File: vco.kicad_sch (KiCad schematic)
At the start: 84 parts, among them J2 Conn_01x18_Pin, Q5 PN2222A, Q6 BC309, Q7 BC309, Q8 BC239, SW2 SW_Rotary_1x3_MP, U10 4013, U14 74LS221, U16 LF353, U20 LF351N, U21 LM301, U22 LM301, U23 LM741

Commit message: Extract keyboard
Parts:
- removed C28: 22uF, symbol Device:C_Polarized
- removed C29: 0.1uF, symbol Device:C
- removed J2: Conn_01x18_Pin, symbol Connector:Conn_01x20_Pin
- removed R73: 33R, symbol Device:R
- removed R74: 100R, symbol Device:R
- removed R75: 3K3, symbol Device:R
- removed RV23: 22K, symbol Device:R_Potentiometer_Trim
- removed U17: ~, symbol Analog:SGS-M110
- RV22: value R_Potentiometer -> 100KA
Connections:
- net +12V: now also U21.7 (V+)
- net -12V: now also U21.4 (V-)
- net at U21.1 (BAL): now also C37.2
- net 2': now reaches U18.2
- net 4': now reaches U18.3
- net 8': now reaches U18.4
- net 16': now reaches U18.5
- net at R95.1: now also U18.9; no longer U18.8
- net at R94.1: now also U18.8; no longer U18.9
- net DC: now reaches Q6.1 (C), Q6.2 (B), Q7.2 (B)
- net at R92.1: now also U18.7; no longer U18.10
- no-connect marks 22 -> 16
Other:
- note added: "5% PWM"
- note added: "CLOCK"
- note added: "LINEARITY"
- note added: "WAVEFORM"
- note removed: "V.REG."
- moved on the sheet: C24, C25, C26, C27, C30, C31, C32, C33, C34, C35, C36, C37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

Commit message: Add missing values and connectors
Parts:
- removed U23: LM741, symbol Amplifier_Operational:LM741
- added J7: Conn_01x11_Pin, symbol Connector:Conn_01x11_Pin
- added U26: LM741, symbol PCM_Amplifier_Operational_AKL:OPAMP_8-pin_Generic
- C24, C25: value C -> 22pF
- R100, R102: value 100K -> 10K
- R70, R90: value 10R -> 10K
- R72: value 36K -> 5K6
- R84: value 47K -> 10K
- R85, R86: value 47K -> 100K
- RV30: value 100KA -> 10KA
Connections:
- net +12V: now also R85.1, J7.1 (Pin_1), U26.7 (V+); no longer R85.2
- net +5V: now also J7.2 (Pin_2)
- net -12V: now also J7.4 (Pin_4), U26.4 (V-)
- net 16': now also J7.11 (Pin_11)
- net 2': now also J7.8 (Pin_8)
- net 4': now also J7.9 (Pin_9)
- net 8': now also J7.10 (Pin_10)
- net CLOCK: now also J7.5 (Pin_5)
- net DC: now also J7.7 (Pin_7)
- net GLIDE: now also J7.6 (Pin_6)
- net GND: now also C31.2, R102.1, J7.3 (Pin_3); no longer C31.1, R102.2
- net at R100.2, R101.1: now also U26.6
- net at R84.2, R86.2, U20.3 (+): now also R85.2; no longer R85.1
- net at R101.2, R103.2, R104.2: now also U26.2 (-)
- net at R69.1, R70.2, U14.7 (RCext): now also C25.2; no longer C25.1
- net at U14.6 (Cext): now also C25.1; no longer C25.2
- net at R77.2, U10.2 (~{Q}): now also C35.1, R90.2
- net PWM renamed PULSE
- new net: C31.1, R77.1, U10.6 (S)
- new net: R102.2, U26.3 (+)
- no-connect marks 16 -> 14
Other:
- note added: "GLIDE"
- note added: "PULSE WIDTH"
- moved on the sheet: C24, C25, C26, C27, C30, C31, C32, C33, C34, C35, C36, D9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

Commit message: Assign footprints and start PCB
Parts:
- C24, C25, C26, C30, C31, C32, C33, C34, C35, C36, C37: footprint (none) -> Capacitor_THT:C_Disc_D5.0mm_W2.5mm_P5.00mm
- CP27: renamed from C27; footprint (none) -> Capacitor_THT:CP_Radial_D8.0mm_P3.80mm
- J7: footprint (none) -> Connector_PinHeader_2.54mm:PinHeader_1x11_P2.54mm_Vertical
- R100, R101, R102, R103, R104, R105, R65, R66, R67, R68, R69, R70, R71, R72, R76, R77, R78, R79, R80, R81, R82, R83, R84, R85, R86, R87, R88, R89, R90, R91, R92, R93, R94, R95, R96, R97, R98, R99: footprint (none) -> Resistor_THT:R_Axial_DIN0204_L3.6mm_D1.6mm_P7.62mm_Horizontal
- RT20: renamed from RV20; footprint (none) -> Potentiometer_THT:Potentiometer_Bourns_3339P_Vertical_HandSoldering
- RT21: renamed from RV21; footprint (none) -> Potentiometer_THT:Potentiometer_Bourns_3339P_Vertical_HandSoldering
- RT26: renamed from RV26; footprint (none) -> Potentiometer_THT:Potentiometer_Bourns_3339P_Vertical_HandSoldering
- RT27: renamed from RV27; footprint (none) -> Potentiometer_THT:Potentiometer_Bourns_3339P_Vertical_HandSoldering
- RT28: renamed from RV28; footprint (none) -> Potentiometer_THT:Potentiometer_Bourns_3339P_Vertical_HandSoldering
- RV19, RV22, RV24, RV25, RV29, RV30: footprint (none) -> Potentiometer_THT:Potentiometer_Omeg_PC16BU_Vertical
- SW2: footprint (none) -> Button_Switch_THT:SR2511F-0403-(L)K0A-C9-S-3_1
- SW40: renamed from U18; value ~ -> 2P4T; footprint (none) -> Button_Switch_THT:SR2511F-0204-(L)K0A-C9-S-3
- U10: footprint (none) -> Package_DIP:DIP-14_W7.62mm_LongPads
- U14: footprint (none) -> Package_DIP:DIP-16_W10.16mm_LongPads
- U16, U26: footprint (none) -> Package_DIP:DIP-8_W7.62mm_LongPads
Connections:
- net GLIDE: no longer J7.6 (Pin_6)
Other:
- note added: "LEVEL"

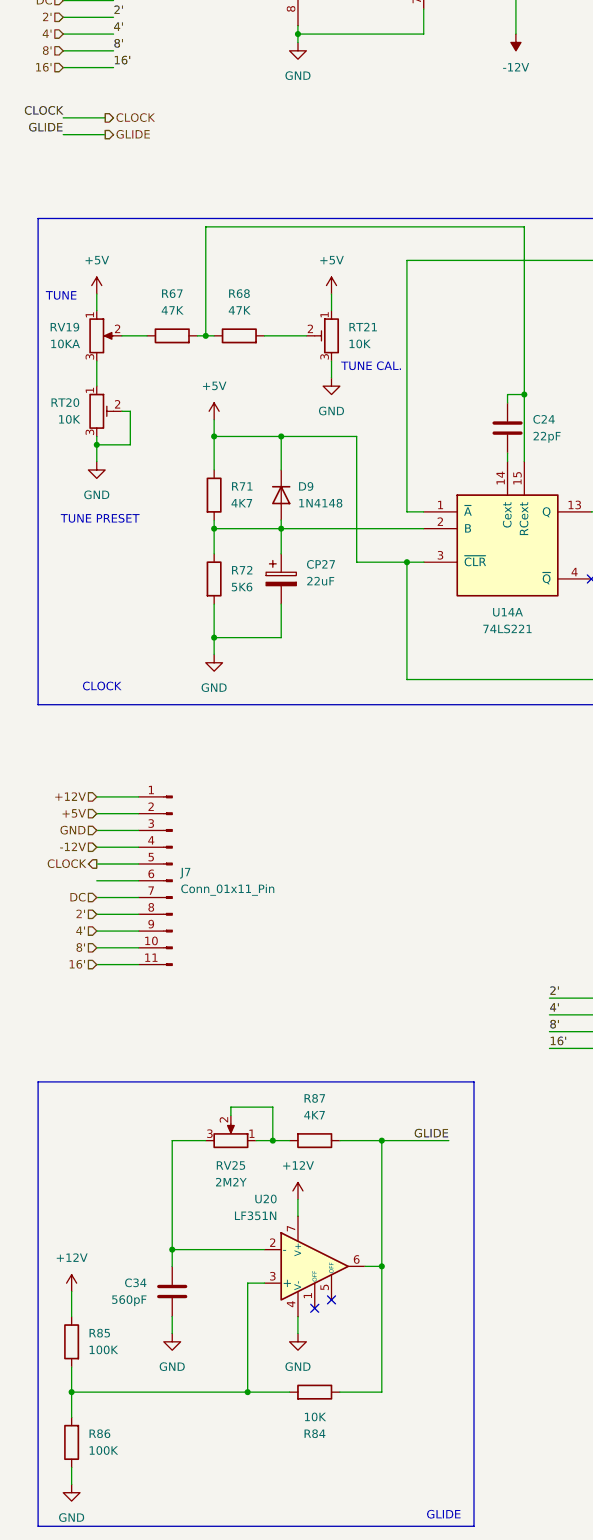
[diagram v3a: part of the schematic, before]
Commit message: Added layout photos, noise & ADSR components are in position
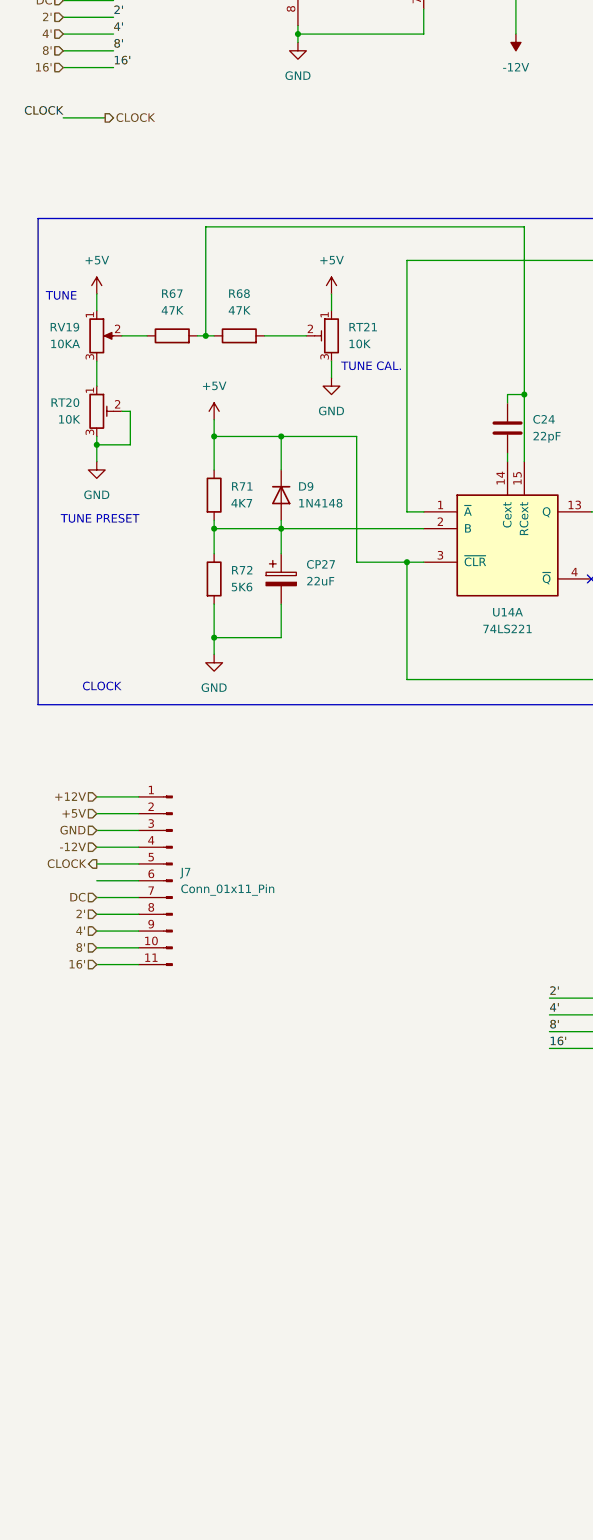
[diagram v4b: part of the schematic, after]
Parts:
- removed C34: 560pF, Capacitor_THT:C_Disc_D5.0mm_W2.5mm_P5.00mm, symbol Device:C
- removed R84: 10K, Resistor_THT:R_Axial_DIN0204_L3.6mm_D1.6mm_P7.62mm_Horizontal, symbol Device:R
- removed R85, R86: 100K, Resistor_THT:R_Axial_DIN0204_L3.6mm_D1.6mm_P7.62mm_Horizontal, symbol Device:R
- removed R87: 4K7, Resistor_THT:R_Axial_DIN0204_L3.6mm_D1.6mm_P7.62mm_Horizontal, symbol Device:R
- removed RV25: 2M2Y, Potentiometer_THT:Potentiometer_Omeg_PC16BU_Vertical, symbol Device:R_Potentiometer
- removed U20: LF351N, PCM_Package_DIP_AKL:DIP-8_W7.62mm_LongPads, symbol PCM_Amplifier_Operational_AKL:LF351N
- R98: footprint Resistor_THT:R_Axial_DIN0204_L3.6mm_D1.6mm_P7.62mm_Horizontal -> Resistor_THT:R_Axial_DIN0207_L6.3mm_D2.5mm_P15.24mm_Horizontal
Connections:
- no-connect marks 14 -> 12
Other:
- note removed: "GLIDE"

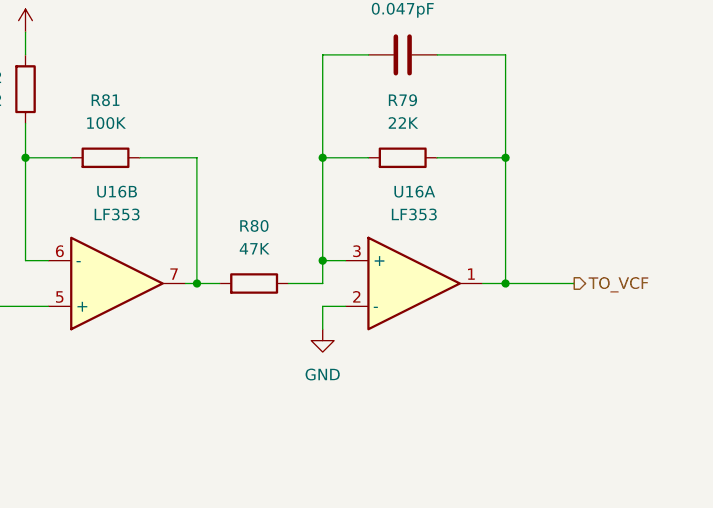
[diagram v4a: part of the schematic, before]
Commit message: VCO components are in position
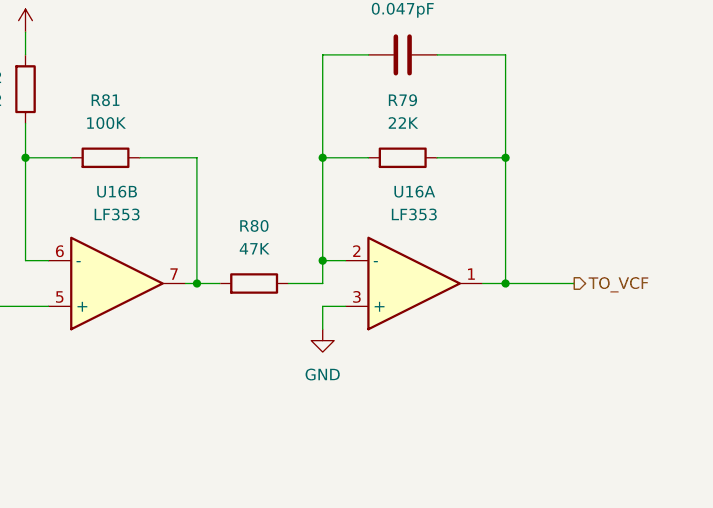
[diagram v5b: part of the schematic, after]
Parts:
- C26, C33, C35, C36: footprint Capacitor_THT:C_Disc_D5.0mm_W2.5mm_P5.00mm -> Capacitor_THT:C_Rect_L11.0mm_W2.8mm_P10.00mm_MKT
- Q5: footprint Package_TO_SOT_THT:TO-92_Inline -> Package_TO_SOT_THT:TO-92_Inline_Wide
- R100, R102, R103, R104, R105, R65, R66, R67, R68, R69, R72, R76, R77, R79, R80, R83, R88, R89, R90, R91, R92, R93, R94, R95, R96, R97, R99: footprint Resistor_THT:R_Axial_DIN0204_L3.6mm_D1.6mm_P7.62mm_Horizontal -> Resistor_THT:R_Axial_DIN0207_L6.3mm_D2.5mm_P15.24mm_Horizontal
- R101, R71, R78, R81, R82: footprint Resistor_THT:R_Axial_DIN0204_L3.6mm_D1.6mm_P7.62mm_Horizontal -> Resistor_THT:R_Axial_DIN0309_L9.0mm_D3.2mm_P12.70mm_Horizontal
- R70: footprint Resistor_THT:R_Axial_DIN0204_L3.6mm_D1.6mm_P7.62mm_Horizontal -> Resistor_THT:R_Axial_DIN0207_L6.3mm_D2.5mm_P10.16mm_Horizontal
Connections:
- net GND: now also U16.3 (+); no longer U16.2 (-)
- net at C33.1, R79.2, R80.1: now also U16.2 (-); no longer U16.3 (+)
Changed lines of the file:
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@@
 			)
 		)
-		(property "Footprint" "Resistor_THT:R_Axial_DIN0204_L3.6mm_D1.6mm_P7.62mm_Horizontal"
+		(property "Footprint" "Resistor_THT:R_Axial_DIN0309_L9.0mm_D3.2mm_P12.70mm_Horizontal"
 			(at 185.928 210.82 90)
 			(effects
@@
 			)
 		)
-		(property "Footprint" "Resistor_THT:R_Axial_DIN0204_L3.6mm_D1.6mm_P7.62mm_Horizontal"
+		(property "Footprint" "Resistor_THT:R_Axial_DIN0207_L6.3mm_D2.5mm_P15.24mm_Horizontal"
 			(at 318.77 122.428 90)
 			(effects
@@
 			)
 		)
-		(property "Footprint" "Resistor_THT:R_Axial_DIN0204_L3.6mm_D1.6mm_P7.62mm_Horizontal"
+		(property "Footprint" "Resistor_THT:R_Axial_DIN0207_L6.3mm_D2.5mm_P15.24mm_Horizontal"
 			(at 45.72 102.108 90)
 			(effects
@@
 			)
 		)
-		(property "Footprint" "Resistor_THT:R_Axial_DIN0204_L3.6mm_D1.6mm_P7.62mm_Horizontal"
+		(property "Footprint" "Resistor_THT:R_Axial_DIN0207_L6.3mm_D2.5mm_P15.24mm_Horizontal"
 			(at 281.94 126.238 90)
 			(effects
@@
 			)
 		)
-		(property "Footprint" "Resistor_THT:R_Axial_DIN0204_L3.6mm_D1.6mm_P7.62mm_Horizontal"
+		(property "Footprint" "Resistor_THT:R_Axial_DIN0207_L6.3mm_D2.5mm_P15.24mm_Horizontal"
 			(at 128.778 193.04 90)
 			(effects
@@
 			)
 		)
-		(property "Footprint" "Resistor_THT:R_Axial_DIN0204_L3.6mm_D1.6mm_P7.62mm_Horizontal"
+		(property "Footprint" "Resistor_THT:R_Axial_DIN0207_L6.3mm_D2.5mm_P15.24mm_Horizontal"
 			(at 243.84 89.408 90)
 			(effects
@@
 			)
 		)
-		(property "Footprint" "Resistor_THT:R_Axial_DIN0204_L3.6mm_D1.6mm_P7.62mm_Horizontal"
+		(property "Footprint" "Resistor_THT:R_Axial_DIN0207_L6.3mm_D2.5mm_P15.24mm_Horizontal"
 			(at 323.088 90.17 90)
 			(effects
@@
 			)
 		)
-		(property "Footprint" "Resistor_THT:R_Axial_DIN0204_L3.6mm_D1.6mm_P7.62mm_Horizontal"
+		(property "Footprint" "Resistor_THT:R_Axial_DIN0207_L6.3mm_D2.5mm_P15.24mm_Horizontal"
 			(at 367.03 116.332 90)
 			(effects
@@
 			)
 		)
-		(property "Footprint" "Resistor_THT:R_Axial_DIN0204_L3.6mm_D1.6mm_P7.62mm_Horizontal"
+		(property "Footprint" "Resistor_THT:R_Axial_DIN0207_L6.3mm_D2.5mm_P15.24mm_Horizontal"
 			(at 233.68 84.328 90)
 			(effects
@@
 			)
 		)
-		(property "Footprint" "Capacitor_THT:C_Disc_D5.0mm_W2.5mm_P5.00mm"
+		(property "Footprint" "Capacitor_THT:C_Rect_L11.0mm_W2.8mm_P10.00mm_MKT"
 			(at 378.46 174.2948 0)
 			(effects
@@
 			)
 		)
-		(property "Footprint" "Resistor_THT:R_Axial_DIN0204_L3.6mm_D1.6mm_P7.62mm_Horizontal"
+		(property "Footprint" "Resistor_THT:R_Axial_DIN0207_L6.3mm_D2.5mm_P15.24mm_Horizontal"
 			(at 243.84 86.868 90)
 			(effects
@@
 			)
 		)
-		(property "Footprint" "Resistor_THT:R_Axial_DIN0204_L3.6mm_D1.6mm_P7.62mm_Horizontal"
+		(property "Footprint" "Resistor_THT:R_Axial_DIN0207_L6.3mm_D2.5mm_P15.24mm_Horizontal"
 			(at 374.65 188.468 90)
 			(effects
@@
 			)
 		)
-		(property "Footprint" "Resistor_THT:R_Axial_DIN0204_L3.6mm_D1.6mm_P7.62mm_Horizontal"
+		(property "Footprint" "Resistor_THT:R_Axial_DIN0207_L6.3mm_D2.5mm_P15.24mm_Horizontal"
 			(at 280.67 84.328 90)
 			(effects
@@
 			)
 		)
-		(property "Footprint" "Resistor_THT:R_Axial_DIN0204_L3.6mm_D1.6mm_P7.62mm_Horizontal"
+		(property "Footprint" "Resistor_THT:R_Axial_DIN0207_L6.3mm_D2.5mm_P15.24mm_Horizontal"
 			(at 353.568 132.08 90)
 			(effects
@@
 			)
 		)
-		(property "Footprint" "Capacitor_THT:C_Disc_D5.0mm_W2.5mm_P5.00mm"
+		(property "Footprint" "Capacitor_THT:C_Rect_L11.0mm_W2.8mm_P10.00mm_MKT"
 			(at 227.33 188.2648 0)
 			(effects
@@
 			)
 		)
-		(property "Footprint" "Resistor_THT:R_Axial_DIN0204_L3.6mm_D1.6mm_P7.62mm_Horizontal"
+		(property "Footprint" "Resistor_THT:R_Axial_DIN0207_L6.3mm_D2.5mm_P15.24mm_Horizontal"
 			(at 325.12 201.422 90)
 			(effects
@@
 			)
 		)
-		(property "Footprint" "Resistor_THT:R_Axial_DIN0204_L3.6mm_D1.6mm_P7.62mm_Horizontal"
+		(property "Footprint" "Resistor_THT:R_Axial_DIN0207_L6.3mm_D2.5mm_P15.24mm_Horizontal"
 			(at 35.56 102.108 90)
 			(effects
@@
 			)
 		)
-		(property "Footprint" "Resistor_THT:R_Axial_DIN0204_L3.6mm_D1.6mm_P7.62mm_Horizontal"
+		(property "Footprint" "Resistor_THT:R_Axial_DIN0207_L6.3mm_D2.5mm_P15.24mm_Horizontal"
 			(at 40.132 137.16 90)
 			(effects
@@
 			)
 		)
-		(property "Footprint" "Resistor_THT:R_Axial_DIN0204_L3.6mm_D1.6mm_P7.62mm_Horizontal"
+		(property "Footprint" "Resistor_THT:R_Axial_DIN0207_L6.3mm_D2.5mm_P15.24mm_Horizontal"
 			(at 304.292 184.15 90)
 			(effects
@@
 			)
 		)
-		(property "Footprint" "Resistor_THT:R_Axial_DIN0204_L3.6mm_D1.6mm_P7.62mm_Horizontal"
+		(property "Footprint" "Resistor_THT:R_Axial_DIN0207_L6.3mm_D2.5mm_P10.16mm_Horizontal"
 			(at 109.22 99.568 90)
 			(effects
@@
 			)
 		)
-		(property "Footprint" "Resistor_THT:R_Axial_DIN0204_L3.6mm_D1.6mm_P7.62mm_Horizontal"
+		(property "Footprint" "Resistor_THT:R_Axial_DIN0309_L9.0mm_D3.2mm_P12.70mm_Horizontal"
 			(at 341.63 188.468 90)
 			(effects
@@
 			)
 		)
-		(property "Footprint" "Resistor_THT:R_Axial_DIN0204_L3.6mm_D1.6mm_P7.62mm_Horizontal"
+		(property "Footprint" "Resistor_THT:R_Axial_DIN0207_L6.3mm_D2.5mm_P15.24mm_Horizontal"
 			(at 287.782 172.72 90)
 			(effects
@@
 			)
 		)
-		(property "Footprint" "Resistor_THT:R_Axial_DIN0204_L3.6mm_D1.6mm_P7.62mm_Horizontal"
+		(property "Footprint" "Resistor_THT:R_Axial_DIN0207_L6.3mm_D2.5mm_P15.24mm_Horizontal"
 			(at 140.97 138.938 90)
 			(effects
@@
 			)
 		)
-		(property "Footprint" "Resistor_THT:R_Axial_DIN0204_L3.6mm_D1.6mm_P7.62mm_Horizontal"
+		(property "Footprint" "Resistor_THT:R_Axial_DIN0309_L9.0mm_D3.2mm_P12.70mm_Horizontal"
 			(at 40.132 124.46 90)
 			(effects
@@
 			)
 		)
-		(property "Footprint" "Resistor_THT:R_Axial_DIN0204_L3.6mm_D1.6mm_P7.62mm_Horizontal"
+		(property "Footprint" "Resistor_THT:R_Axial_DIN0207_L6.3mm_D2.5mm_P15.24mm_Horizontal"
 			(at 146.05 99.568 90)
 			(effects
@@
 			)
 		)
-		(property "Footprint" "Resistor_THT:R_Axial_DIN0204_L3.6mm_D1.6mm_P7.62mm_Horizontal"
+		(property "Footprint" "Resistor_THT:R_Axial_DIN0309_L9.0mm_D3.2mm_P12.70mm_Horizontal"
 			(at 340.36 104.648 90)
 			(effects
@@
 			)
 		)
-		(property "Footprint" "Resistor_THT:R_Axial_DIN0204_L3.6mm_D1.6mm_P7.62mm_Horizontal"
+		(property "Footprint" "Resistor_THT:R_Axial_DIN0309_L9.0mm_D3.2mm_P12.70mm_Horizontal"
 			(at 330.962 179.07 90)
 			(effects
@@
 			)
 		)
-		(property "Footprint" "Capacitor_THT:C_Disc_D5.0mm_W2.5mm_P5.00mm"
+		(property "Footprint" "Capacitor_THT:C_Rect_L11.0mm_W2.8mm_P10.00mm_MKT"
 			(at 137.16 149.5552 0)
 			(effects
@@
 			)
 		)
-		(property "Footprint" "Resistor_THT:R_Axial_DIN0204_L3.6mm_D1.6mm_P7.62mm_Horizontal"
+		(property "Footprint" "Resistor_THT:R_Axial_DIN0207_L6.3mm_D2.5mm_P15.24mm_Horizontal"
 			(at 173.228 184.15 90)
 			(effects
@@
 			)
 		)
-		(property "Footprint" "Package_TO_SOT_THT:TO-92_Inline"
+		(property "Footprint" "Package_TO_SOT_THT:TO-92_Inline_Wide"
 			(at 158.75 139.065 0)
 			(effects
@@
 			)
 		)
-		(property "Footprint" "Resistor_THT:R_Axial_DIN0204_L3.6mm_D1.6mm_P7.62mm_Horizontal"
+		(property "Footprint" "Resistor_THT:R_Axial_DIN0207_L6.3mm_D2.5mm_P15.24mm_Horizontal"
 			(at 207.01 180.848 90)
 			(effects
@@
 			)
 		)
-		(property "Footprint" "Resistor_THT:R_Axial_DIN0204_L3.6mm_D1.6mm_P7.62mm_Horizontal"
+		(property "Footprint" "Resistor_THT:R_Axial_DIN0207_L6.3mm_D2.5mm_P15.24mm_Horizontal"
 			(at 367.03 136.652 90)
 			(effects
@@
 			)
 		)
-		(property "Footprint" "Resistor_THT:R_Axial_DIN0204_L3.6mm_D1.6mm_P7.62mm_Horizontal"
+		(property "Footprint" "Resistor_THT:R_Axial_DIN0207_L6.3mm_D2.5mm_P15.24mm_Horizontal"
 			(at 223.52 177.292 90)
 			(effects
@@
 			)
 		)
-		(property "Footprint" "Capacitor_THT:C_Disc_D5.0mm_W2.5mm_P5.00mm"
+		(property "Footprint" "Capacitor_THT:C_Rect_L11.0mm_W2.8mm_P10.00mm_MKT"
 			(at 253.6952 181.61 0)
 			(effects
@@
 			)
 		)
-		(property "Footprint" "Resistor_THT:R_Axial_DIN0204_L3.6mm_D1.6mm_P7.62mm_Horizontal"
+		(property "Footprint" "Resistor_THT:R_Axial_DIN0207_L6.3mm_D2.5mm_P15.24mm_Horizontal"
 			(at 154.432 124.46 90)
 			(effects
@@
 			)
 		)
-		(property "Footprint" "Resistor_THT:R_Axial_DIN0204_L3.6mm_D1.6mm_P7.62mm_Horizontal"
+		(property "Footprint" "Resistor_THT:R_Axial_DIN0207_L6.3mm_D2.5mm_P15.24mm_Horizontal"
 			(at 262.89 110.998 90)
 			(effects
@@
 			)
 		)
-		(property "Footprint" "Resistor_THT:R_Axial_DIN0204_L3.6mm_D1.6mm_P7.62mm_Horizontal"
+		(property "Footprint" "Resistor_THT:R_Axial_DIN0207_L6.3mm_D2.5mm_P15.24mm_Horizontal"
 			(at 233.68 89.408 90)
 			(effects
@@
 		(lib_id "Device:Opamp_Dual")
 		(at 375.92 200.66 0)
+		(mirror x)
 		(unit 1)
 		(exclude_from_sim no)
@@
 			)
 		)
-		(property "Footprint" "Resistor_THT:R_Axial_DIN0204_L3.6mm_D1.6mm_P7.62mm_Horizontal"
+		(property "Footprint" "Resistor_THT:R_Axial_DIN0207_L6.3mm_D2.5mm_P15.24mm_Horizontal"
 			(at 358.14 202.438 90)
 			(effects

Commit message: Fix PCB sizes, adjust layout to new size
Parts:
- added J4: Conn_01x09_Pin, Connector_PinHeader_2.54mm:PinHeader_1x09_P2.54mm_Vertical, symbol Connector:Conn_01x09_Pin
- added R110: 47k, Resistor_THT:R_Axial_DIN0207_L6.3mm_D2.5mm_P15.24mm_Horizontal, symbol Device:R
- J7: footprint Connector_PinHeader_2.54mm:PinHeader_1x11_P2.54mm_Vertical -> Connector_PinHeader_2.54mm:PinHeader_1x10_P2.54mm_Vertical; symbol Connector:Conn_01x11_Pin -> Connector:Conn_01x10_Pin
- R89: footprint Resistor_THT:R_Axial_DIN0207_L6.3mm_D2.5mm_P15.24mm_Horizontal -> Resistor_THT:R_Axial_DIN0309_L9.0mm_D3.2mm_P12.70mm_Horizontal
- RT20, RT21, RT26, RT27, RT28: footprint Potentiometer_THT:Potentiometer_Bourns_3339P_Vertical_HandSoldering -> Potentiometer_THT:Potentiometer_Piher_PT-10-V10_Vertical
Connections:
- net +12V: now also J7.6 (Pin_6), J4.5 (Pin_5); no longer J7.1 (Pin_1)
- net +5V: now also RV19.3, J4.9 (Pin_9); no longer J7.2 (Pin_2), RV19.1
- net -12V: now also J4.6 (Pin_6); no longer J7.4 (Pin_4)
- net 16': now also J7.4 (Pin_4); no longer J7.11 (Pin_11)
- net 2': now also J7.1 (Pin_1); no longer J7.8 (Pin_8)
- net 4': now also J7.2 (Pin_2); no longer J7.9 (Pin_9)
- net 8': now also J7.3 (Pin_3); no longer J7.10 (Pin_10)
- net CLOCK: now also J7.7 (Pin_7); no longer J7.5 (Pin_5)
- net DC: now also J7.5 (Pin_5); no longer J7.7 (Pin_7)
- net GND: now also J7.8 (Pin_8), RV24.1, J4.7 (Pin_7); no longer J7.3 (Pin_3), RV24.3
- net TO_VCF: now also J4.1 (Pin_1)
- net TO_VCF_INPUT: now also J4.8 (Pin_8), R110.1; no longer RV24.2
- net at SW2.4: now also RV24.3; no longer RV24.1
- net at RT20.1: now also RV19.1; no longer RV19.3
- new net: J4.2 (Pin_2), J7.9 (Pin_9)
- new net: J4.3 (Pin_3), J7.10 (Pin_10)
- new net: R110.2, RV24.2
- new net LFO_OUT: J4.4 (Pin_4)
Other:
- note added: "NOTE: Not on schematic"
- moved on the sheet: C37, D10, R100, R101, R102, R103, R104, R105, R92, R93, R94, R95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
